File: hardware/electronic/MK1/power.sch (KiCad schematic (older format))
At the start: 6 parts

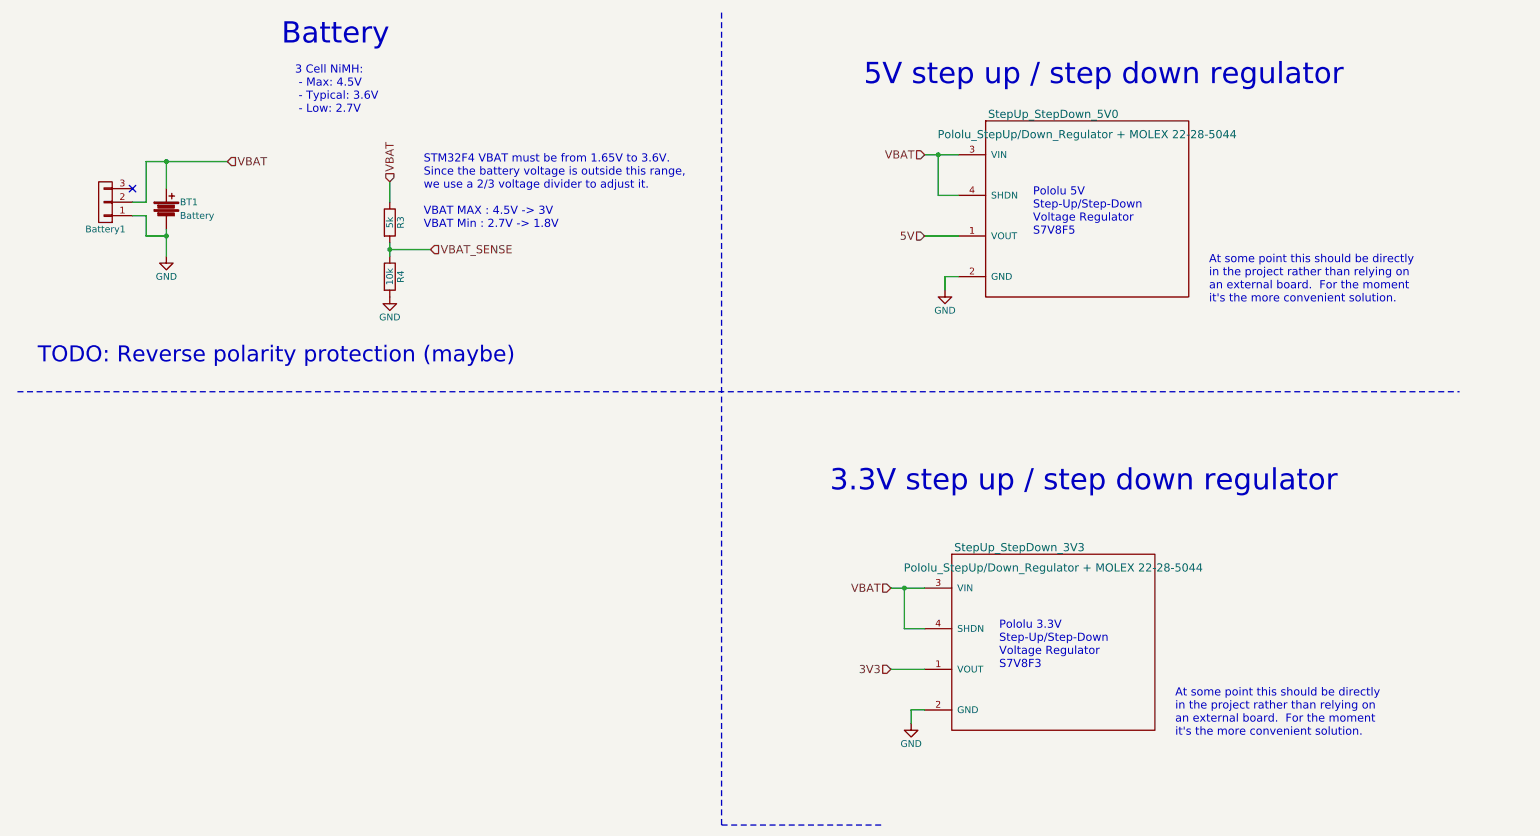
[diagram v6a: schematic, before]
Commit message: HW: Add master switch
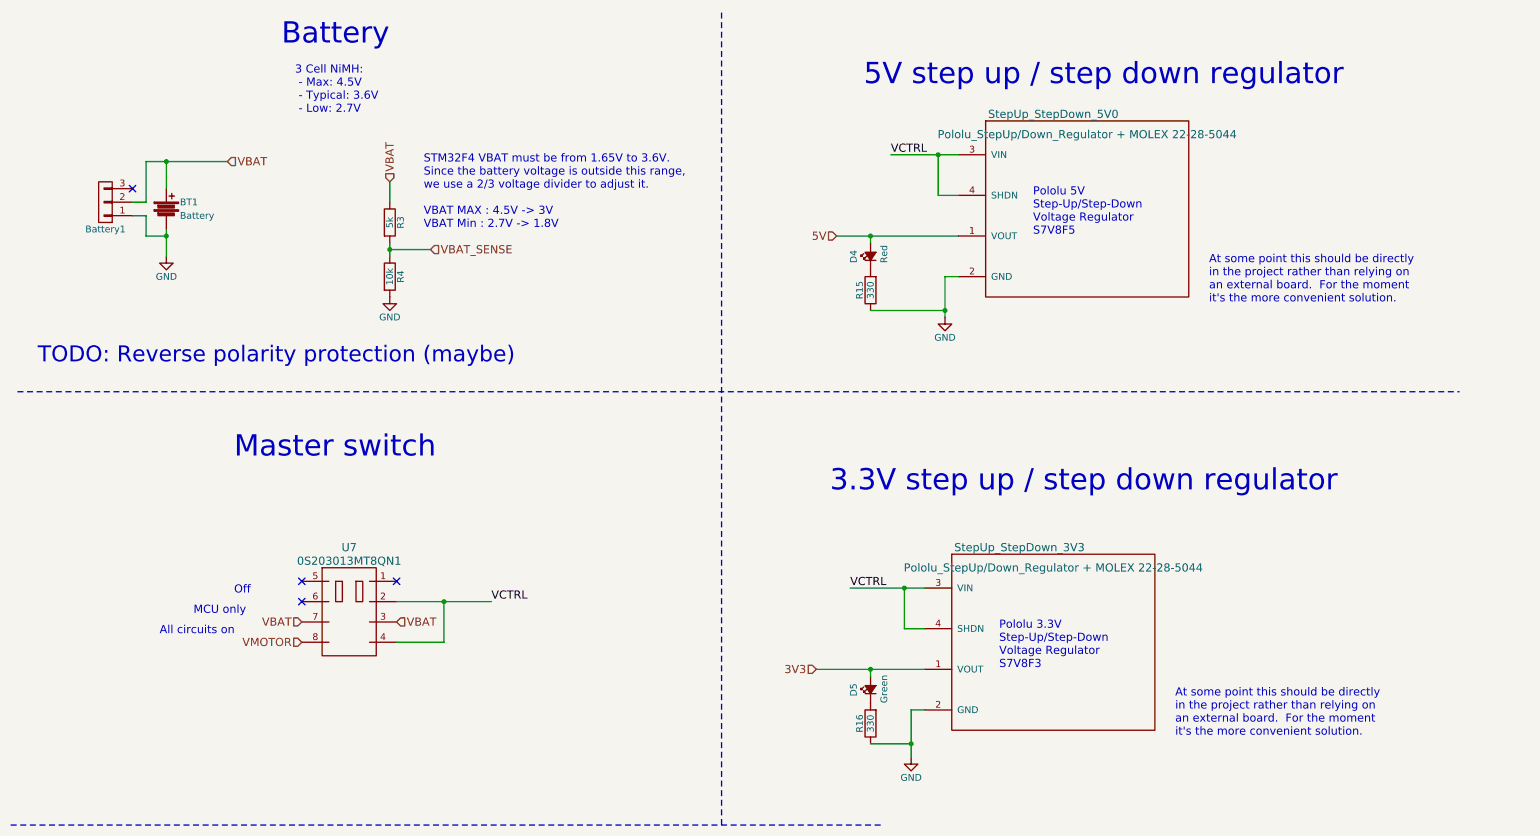
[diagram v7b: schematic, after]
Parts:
- added D4: Red, LEDs:LED_0805, symbol Led_Small
- added D5: Green, LEDs:LED_0805, symbol Led_Small
- added R15, R16: 330, Resistors_SMD:R_0805, symbol R
- added U7: 0S203013MT8QN1, OPAVES_Footprints:DP3T_switch, symbol DP3T_switch
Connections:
- net 3V3: now also D5.2 (A)
- net 5V: now also D4.2 (A)
- net GND: now also R15.1, R16.1
- net VBAT: now also U7.3, U7.7; no longer StepUp_StepDown_3V3.3 (VIN), StepUp_StepDown_3V3.4 (SHDN), StepUp_StepDown_5V0.3 (VIN), StepUp_StepDown_5V0.4 (SHDN)
- new net: D4.1 (K), R15.2
- new net: D5.1 (K), R16.2
- new net VCTRL: StepUp_StepDown_3V3.3 (VIN), StepUp_StepDown_3V3.4 (SHDN), StepUp_StepDown_5V0.3 (VIN), StepUp_StepDown_5V0.4 (SHDN), U7.2, U7.4
- new net VMOTOR: U7.8
- no-connect marks 1 -> 4
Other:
- note added: "All circuits on"
- note added: "MCU only"
- note added: "Master switch"
- note added: "Off"
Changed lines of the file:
@@
 	7500 1900 7350 1900
 Wire Wire Line
-	7500 2200 7250 2200
-Wire Wire Line
-	7400 2500 7400 2600
+	6600 2200 7500 2200
+Wire Wire Line
+	7400 2500 7400 2800
 Wire Wire Line
 	7500 2500 7400 2500
 Wire Wire Line
-	7500 1600 7250 1600
+	7000 1600 7500 1600
 $Comp
 L Pololu_StepUp/Down_Regulator StepUp_StepDown_5V0
@@
 Text Notes 6800 1100 0    157  ~ 0
 5V step up / step down regulator
-Text HLabel 7250 1600 0    60   Input ~ 0
-VBAT
-Text HLabel 7250 2200 0    60   Input ~ 0
+Text HLabel 6600 2200 0    60   Input ~ 0
 5V
 $Comp
 L GND #PWR018
 U 1 1 588A1F16
-P 7400 2600
-F 0 "#PWR018" H 7400 2350 50  0001 C CNN
-F 1 "GND" H 7400 2450 50  0000 C CNN
-F 2 "" H 7400 2600 50  0000 C CNN
-F 3 "" H 7400 2600 50  0000 C CNN
-	1    7400 2600
+P 7400 2800
+F 0 "#PWR018" H 7400 2550 50  0001 C CNN
+F 1 "GND" H 7400 2650 50  0000 C CNN
+F 2 "" H 7400 2800 50  0000 C CNN
+F 3 "" H 7400 2800 50  0000 C CNN
+	1    7400 2800
 	1    0    0    -1
 $EndComp
@@
 	7250 5100 7100 5100
 Wire Wire Line
-	7250 5400 7000 5400
-Wire Wire Line
-	7150 5700 7150 5800
+	6450 5400 7250 5400
+Wire Wire Line
+	7150 5700 7150 6050
 Wire Wire Line
 	7250 5700 7150 5700
 Wire Wire Line
-	7250 4800 7000 4800
+	6700 4800 7250 4800
 $Comp
 L Pololu_StepUp/Down_Regulator StepUp_StepDown_3V3
@@
 Text Notes 6550 4100 0    157  ~ 0
 3.3V step up / step down regulator
-Text HLabel 7000 4800 0    60   Input ~ 0
-VBAT
-Text HLabel 7000 5400 0    60   Input ~ 0
+Text HLabel 6450 5400 0    60   Input ~ 0
 3V3
 $Comp
 L GND #PWR019
 U 1 1 588A6FD6
-P 7150 5800
-F 0 "#PWR019" H 7150 5550 50  0001 C CNN
-F 1 "GND" H 7150 5650 50  0000 C CNN
-F 2 "" H 7150 5800 50  0000 C CNN
-F 3 "" H 7150 5800 50  0000 C CNN
-	1    7150 5800
+P 7150 6050
+F 0 "#PWR019" H 7150 5800 50  0001 C CNN
+F 1 "GND" H 7150 5900 50  0000 C CNN
+F 2 "" H 7150 6050 50  0000 C CNN
+F 3 "" H 7150 6050 50  0000 C CNN
+	1    7150 6050
 	1    0    0    -1
 $EndComp
@@
 	5750 550  5750 6550
 Wire Notes Line
-	5750 6550 6950 6550
+	500  6550 6950 6550
 Wire Wire Line
 	1650 2150 1650 2350
@@
 Text Notes 700  3150 0    118  ~ 0
 TODO: Reverse polarity protection (maybe)
+$Comp
+L Led_Small D4
+U 1 1 58DB4328
+P 6850 2350
+F 0 "D4" H 6800 2475 50  0000 L CNN
+F 1 "Red" H 6800 2250 50  0000 L CNN
+F 2 "LEDs:LED_0805" V 6850 2350 50  0001 C CNN
+F 3 "" V 6850 2350 50  0000 C CNN
+	1    6850 2350
+	0    -1   -1   0
+$EndComp
+$Comp
+L R R15
+U 1 1 58DB4330
+P 6850 2600
+F 0 "R15" V 6930 2600 50  0000 C CNN
+F 1 "330" V 6850 2600 50  0000 C CNN
+F 2 "Resistors_SMD:R_0805" V 6780 2600 50  0001 C CNN
+F 3 "" H 6850 2600 50  0000 C CNN
+	1    6850 2600
+	-1   0    0    1
+$EndComp
+Wire Wire Line
+	7400 2750 6850 2750
+Connection ~ 7400 2750
+Wire Wire Line
+	6850 2250 6850 2200
+Connection ~ 6850 2200
+$Comp
+L Led_Small D5
+U 1 1 58DB4F4F
+P 6850 5550
+F 0 "D5" H 6800 5675 50  0000 L CNN
+F 1 "Green" H 6750 5450 50  0000 L CNN
+F 2 "LEDs:LED_0805" V 6850 5550 50  0001 C CNN
+F 3 "" V 6850 5550 50  0000 C CNN
+	1    6850 5550
+	0    -1   -1   0
+$EndComp
+$Comp
+L R R16
+U 1 1 58DB4F57
+P 6850 5800
+F 0 "R16" V 6930 5800 50  0000 C CNN
+F 1 "330" V 6850 5800 50  0000 C CNN
+F 2 "Resistors_SMD:R_0805" V 6780 5800 50  0001 C CNN
+F 3 "" H 6850 5800 50  0000 C CNN
+	1    6850 5800
+	-1   0    0    1
+$EndComp
+Wire Wire Line
+	6850 5450 6850 5400
+Connection ~ 6850 5400
+Wire Wire Line
+	7150 5950 6850 5950
+Connection ~ 7150 5950
+$Comp
+L DP3T_switch U7
+U 1 1 58DB8591
+P 3000 4500
+F 0 "U7" H 3000 4500 60  0000 C CNN
+F 1 "0S203013MT8QN1" H 3000 4400 60  0000 C CNN
+F 2 "OPAVES_Footprints:DP3T_switch" H 3000 4500 60  0001 C CNN
+F 3 "" H 3000 4500 60  0001 C CNN
+	1    3000 4500
+	1    0    0    -1
+$EndComp
+NoConn ~ 3350 4750
+Text Notes 2150 4850 0    60   ~ 0
+Off
+Text Notes 1850 5000 0    60   ~ 0
+MCU only
+Text Notes 1600 5150 0    60   ~ 0
+All circuits on
+NoConn ~ 2650 4750
+Text HLabel 2650 5200 0    60   Input ~ 0
+VMOTOR
+Text HLabel 2650 5050 0    60   Input ~ 0
+VBAT
+Text HLabel 3350 5050 2    60   Input ~ 0
+VBAT
+Wire Wire Line
+	3350 4900 4050 4900
+Wire Wire Line
+	3700 4900 3700 5200
+Wire Wire Line
+	3700 5200 3350 5200
+NoConn ~ 2650 4900
+Connection ~ 3700 4900
+Text Label 4050 4900 0    60   ~ 0
+VCTRL
+Text Label 7000 1600 0    60   ~ 0
+VCTRL
+Text Label 6700 4800 0    60   ~ 0
+VCTRL
+Text Notes 2150 3850 0    157  ~ 0
+Master switch
 $EndSCHEMATC
